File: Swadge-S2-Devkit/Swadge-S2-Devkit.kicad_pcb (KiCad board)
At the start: 2 copper layers, 134 x 100 mm, 102 parts, among them J1 CurrentMonitor, J10 LCD18, J11 LCD28, J2 DEBUG_BANK_C, J3 DEBUG_BANK_B, J4 DEBUG_BANK_A, J5 MICSEL, J6 TRYMIC, J7 LEDK_J, M1 VZ43FC1B5640007L, P1 USB_C_Plug_USB2.0, Q1 Q_N_FET, Q2 AP2003_PN_FET, Q3 AP2003_PN_FET, Q4 AP2003_PN_FET, SW1 4-1437565-2, SW13 touch-ring-6, SW14 SW_SPDT, SW2 4-1437565-2, SW3 4-1437565-2, SW4 4-1437565-2, SW5 4-1437565-2, SW6 4-1437565-2, SW7 4-1437565-2, SW8 4-1437565-2, SW9 4-1437565-2, U1 ESP32-S2-SOLO, U10 GENERIC_LDO_2.8, U11 LCD_240x240_1.3_12, U12 LCD_135x240_1.14_13, U15 LCD_240x240_1.54_12, U2 BUS_PCIexpress, U3 MT3410, U4 GS321-TR, U5 QMA7981, U6 INGHAi_GSPK2308P-8R0.5W, U7 TFT-1.14, U8 TFT_DISPLAY, U9 GENERIC_LDO_1.8

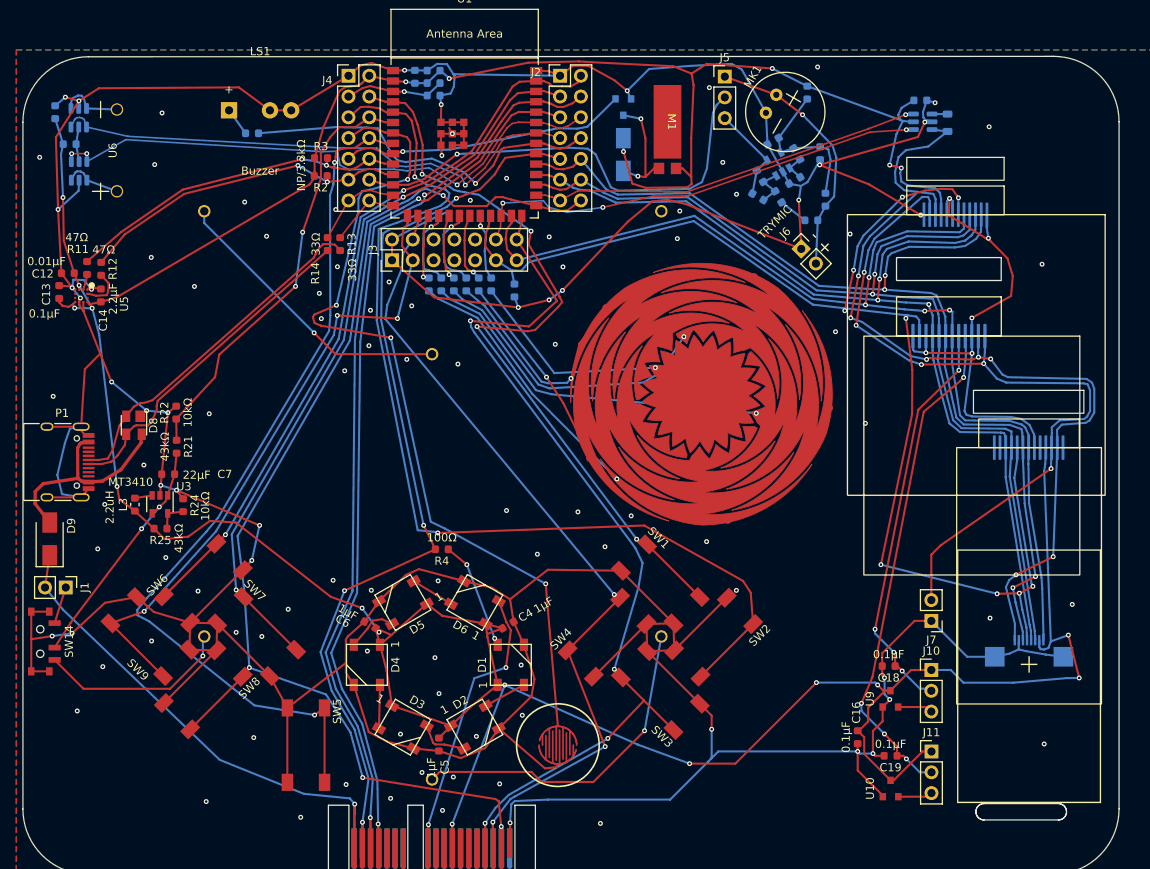
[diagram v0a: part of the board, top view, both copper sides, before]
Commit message: Fixed all import and DRC errors. Cleaned up BOM
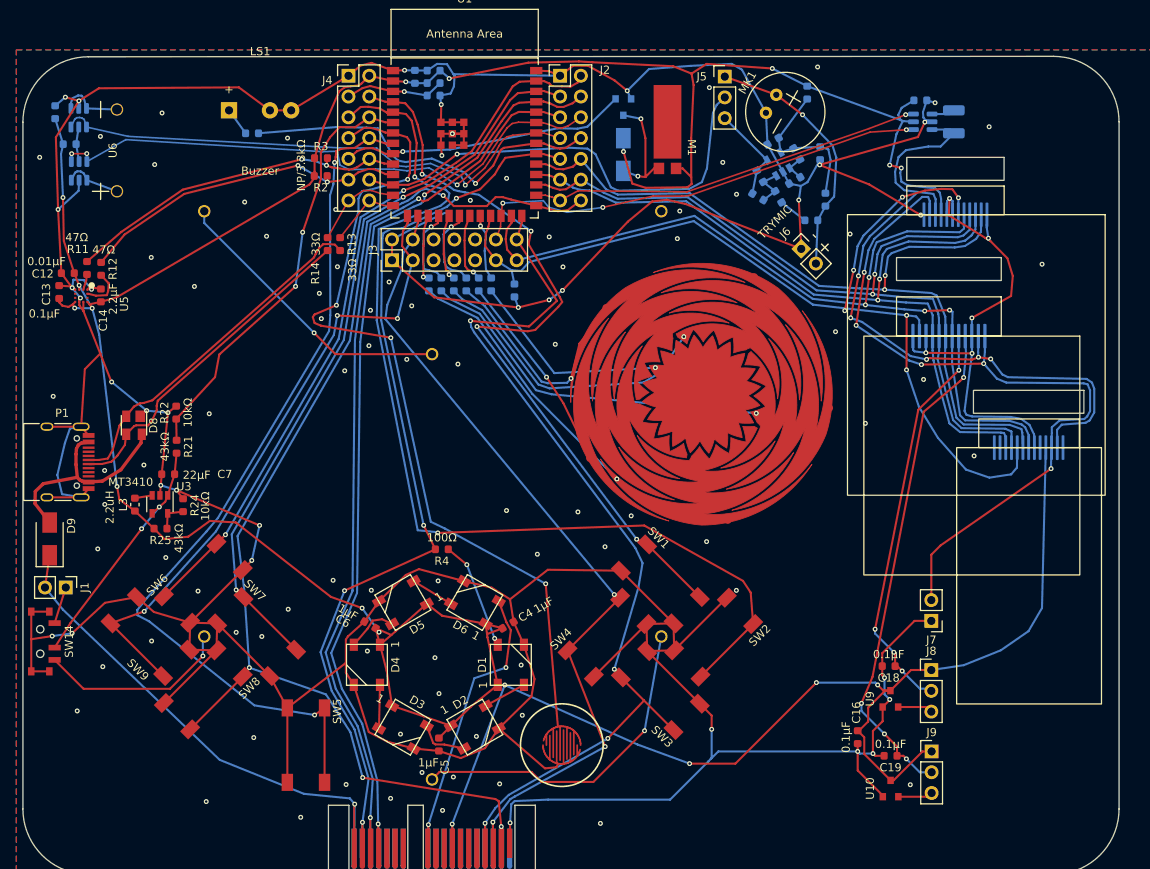
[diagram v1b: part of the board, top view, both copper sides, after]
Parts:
- removed BTN1: BLISTER_SILICONE_BUTTON, Swadge_Parts:BTC007_Button_Silicone
- removed J10: LCD18, Swadge_Parts:PinHeader_1x03_P2.54mm_Vertical
- removed J11: LCD28, Swadge_Parts:PinHeader_1x03_P2.54mm_Vertical
- removed SW13: touch-ring-6, Swadge_Parts:Touch_Teeth_5
- removed U7: TFT-1.14, Swadge_Parts:TFT-1.14
- removed U8: TFT_DISPLAY, Swadge_Parts:NULL
- added J8: LCD18, Swadge_Parts:PinHeader_1x03_P2.54mm_Vertical, F.Cu at (213.4, 126.6)
- added J9: LCD28, Swadge_Parts:PinHeader_1x03_P2.54mm_Vertical, F.Cu at (213.5, 136.6)
- added SW10: BLISTER_SILICONE_BUTTON, Swadge_Parts:BTC007_Button_Silicone, F.Cu at (168.3, 135.8)
- added SW11: touch-ring-6, Swadge_Parts:Touch_Teeth_5, F.Cu at (169.3, 76.9)
- L2: footprint Swadge_Parts:L_0805_2012Metric -> Swadge_Parts:L_1210_3225Metric
- moved L2 0.77 mm to (216.2, 59.6)
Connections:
- P1 pad A8: (no net) -> unconnected-(P1-PadA8)
- P1 pad B6: (no net) -> unconnected-(P1-PadB6)
- P1 pad B7: (no net) -> unconnected-(P1-PadB7)
- P1 pad B8: (no net) -> unconnected-(P1-PadB8)
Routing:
- net TFT_RS: track 165.7 -> 122.8 mm, vias 9 -> 6
- net TFT_RESET: track 125.2 -> 99.7 mm, vias 4 -> 2
- net TFT_LEDA: track 111.4 -> 86.2 mm, vias 7 -> 5
- net TFT_SDA: track 120.2 -> 96.2 mm, vias 3 -> 2
- net TFT_SCL: track 121.0 -> 97.2 mm
- net TFT_CS: track 131.4 -> 107.7 mm
- net GND: track 795.9 -> 775.8 mm, vias 116 -> 119
- net +3V3: track 475.4 -> 458.1 mm, vias 20 -> 18
- net Net-(L2-Pad1): track 1.90 -> 2.85 mm

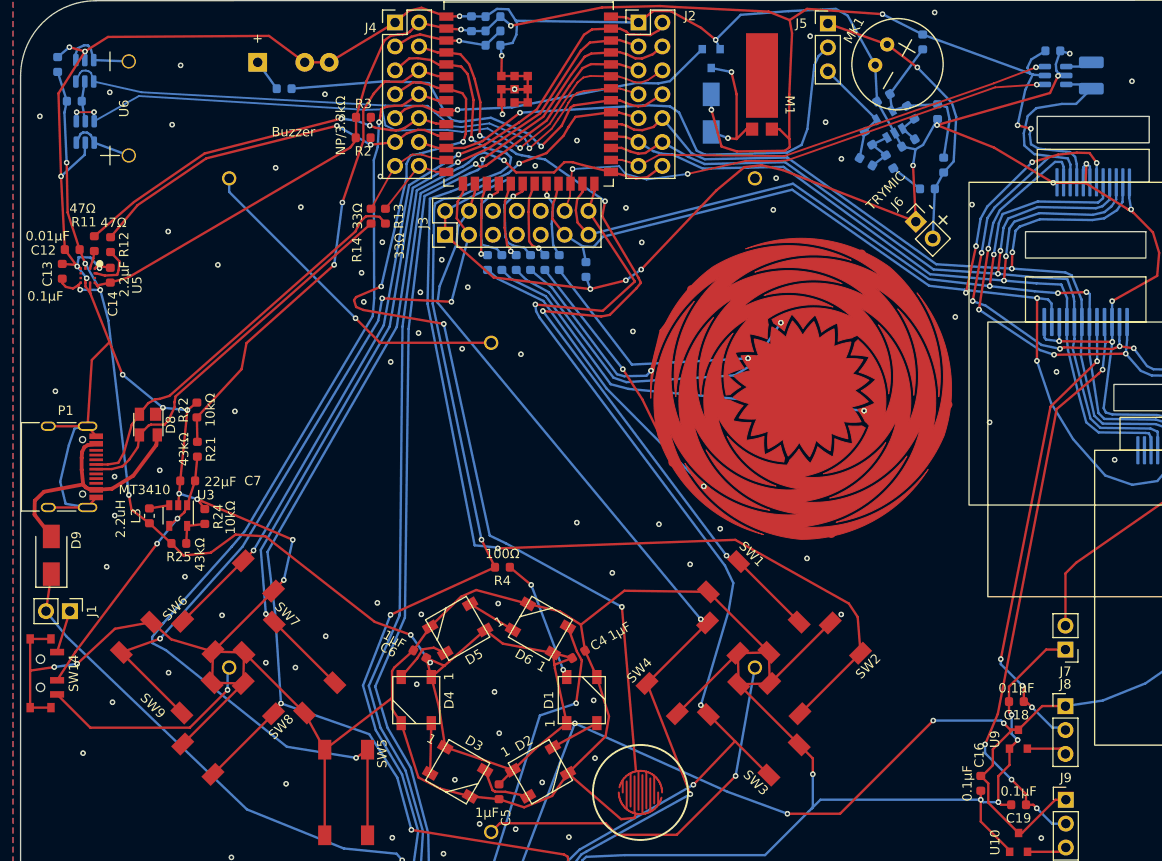
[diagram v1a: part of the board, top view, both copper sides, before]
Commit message: Switch inductors, fix warnings
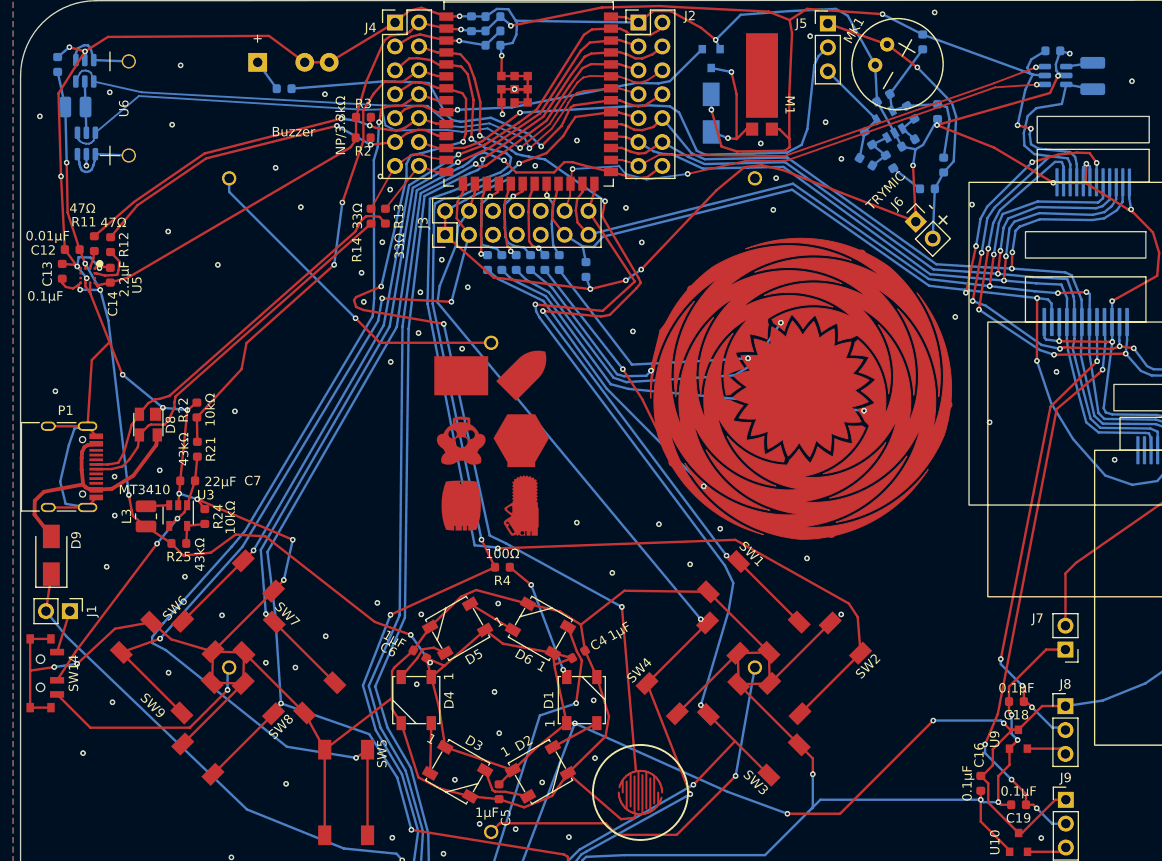
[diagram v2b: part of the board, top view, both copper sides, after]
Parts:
- added Ref**: Val**, Swadge_Parts:swadges-family, F.Cu at (152.5, 98.7)
- L1, L3: footprint Swadge_Parts:L_0603_1608Metric -> Swadge_Parts:L_1008_2520Metric
- moved Q3 1.23 mm to (109.4, 66.8)
- moved L1 0.63 mm to (108.2, 62.9)
- moved L3 0.36 mm to (115.7, 106.5)
- moved L2 0.16 mm to (216.3, 59.7)
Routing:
- net GND: track 775.8 -> 772.3 mm, vias 119 -> 121
- net TFT_LEDA: track 86.2 -> 84.5 mm
- net DIPRAIL: track 4.28 -> 5.45 mm
- net Net-(Q3-Pad4): track 7.05 -> 8.19 mm
- net SP+: track 71.0 -> 71.3 mm, vias 3 -> 1

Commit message: Update note for manufacturing Add silkscreen version Ignore output folder
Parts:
- added svg2mod: G***, Swadge_Parts:MAGFEST_logo_centered_final, F.Cu at (177.1, 146.6)
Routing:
- net GND: vias 121 -> 122
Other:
- board text added: "Swadge S2 Devkit 1.0.0"

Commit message: Reset PCB
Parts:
- removed C12: 0.01μF, Swadge_Parts:C_0603_1608Metric
- removed C13: 0.1μF, Swadge_Parts:C_0603_1608Metric
- removed C14: 2.2μF, Swadge_Parts:C_0603_1608Metric
- removed C15: 10μF, Swadge_Parts:C_0603_1608Metric
- removed D7: D, Swadge_Parts:D_SMA
- removed J1: CurrentMonitor, Swadge_Parts:PinHeader_1x02_P2.54mm_Vertical
- removed J2: DEBUG_BANK_C, Swadge_Parts:PinHeader_2x07_P2.54mm_Vertical
- removed J3: DEBUG_BANK_B, Swadge_Parts:PinHeader_2x07_P2.54mm_Vertical
- removed J4: DEBUG_BANK_A, Swadge_Parts:PinHeader_2x07_P2.54mm_Vertical
- removed L1: 2.2uH, Swadge_Parts:L_1008_2520Metric
- removed M1: VZ43FC1B5640007L, Swadge_Parts:VZ43FC1B5640007L
- removed Q1: Q_N_FET, Swadge_Parts:SOT-23
- removed Q2, Q3: AP2003_PN_FET, Swadge_Parts:SOT-23-6
- removed R11, R12: 47Ω, Swadge_Parts:R_0603_1608Metric
- removed R2, R3: NP/3.3kΩ, Swadge_Parts:R_0603_1608Metric
- removed Ref**: Val**, Swadge_Parts:swadges-family
- removed SW10: BLISTER_SILICONE_BUTTON, Swadge_Parts:BTC007_Button_Silicone
- removed SW14: SW_SPDT, Swadge_Parts:SW_SPDT_PCM12
- removed SW8, SW9: 4-1437565-2, Swadge_Parts:SW_4-1437565-2
- removed U2: BUS_PCIexpress, Swadge_Parts:BUS_PCIexpress
- removed U5: QMA7981, Swadge_Parts:QMA6981
- removed U6: INGHAi_GSPK2308P-8R0.5W, Swadge_Parts:INGHAi GSPK2308P-8R0.5W
- removed svg2mod: G***, Swadge_Parts:MAGFEST_logo_centered_final
- BT1, BT2, BT3, C1, C10, C11, C17, C2, C3, C8, C9, L2, Q4, R1, R10, R15, R16, R17, R18, R19, R20, R23, R26, R5, R6, R7, R8, R9, U11, U12, U15, U4: moved to F.Cu
- SW1, SW2, SW3, SW4, SW5, SW6: value 4-1437565-2 -> EVQ-Q2B03W; footprint Swadge_Parts:SW_4-1437565-2 -> Swadge_Parts:EVQ-Q2B03W
- SW7: value 4-1437565-2 -> SW_SPDT_1825232-1; footprint Swadge_Parts:SW_4-1437565-2 -> Swadge_Parts:1825232-1
- moved L2 158.3 mm to (76.1, 133.1), turned to 0 degrees
- moved Q4 150.2 mm to (81.5, 133.2)
- moved C17 144.1 mm to (90.1, 133.5)
- moved U15 133.5 mm to (84.1, 89.0), turned to 0 degrees
- moved C9 126.9 mm to (94.1, 133.5), turned to 0 degrees
- moved R9 125.9 mm to (86.1, 133.5), turned to 0 degrees
- moved U12 118.5 mm to (107.3, 89.0), turned to 0 degrees
- moved J9 108.3 mm to (119.0, 83.7)
- moved J8 100.1 mm to (119.0, 93.4)
- moved SW1 99.2 mm to (81.7, 127.4), turned to 0 degrees
- moved D5 99.0 mm to (218.9, 48.5), turned to 0 degrees
- moved U4 91.1 mm to (124.8, 123.2), turned to 0 degrees
- moved C11 89.2 mm to (124.4, 126.7), turned to 0 degrees
- moved BT2 83.3 mm to (94.3, 54.3), turned to 0 degrees
- moved C16 82.7 mm to (217.0, 53.0), turned to 0 degrees
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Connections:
- P1 pad B6: unconnected-(P1-PadB6) -> Net-(D8-Pad2)
- P1 pad B7: unconnected-(P1-PadB7) -> Net-(D8-Pad3)
- SW7 pad 1: BTN_7 -> +5V
- SW7 pad 2: BTN_7 -> Net-(C7-Pad1)
- SW7 pad 3: GND -> BATTPLUS
- U1 pad 10: SDA -> unconnected-(U1-Pad10)
- U1 pad 11: SCL -> unconnected-(U1-Pad11)
- U1 pad 15: BTN_9 -> BTN_4
- U1 pad 16: BTN_4 -> unconnected-(U1-Pad16)
- U1 pad 26: BTN_3 -> unconnected-(U1-Pad26)
- U1 pad 27: BTN_8 -> BTN_1
- U1 pad 34: SP- -> unconnected-(U1-Pad34)
- U1 pad 35: SP+ -> unconnected-(U1-Pad35)
- U1 pad 38: BTN_7 -> BTN_3
- U1 pad 39: BTN_6 -> BTN_2
- U1 pad 4: BTN_1 -> BTN_5
- U1 pad 5: BTN_2 -> BTN_6
- U1 pad 7: BLISTER1 -> unconnected-(U1-Pad7)
- U1 pad 8: BTN_5 -> unconnected-(U1-Pad8)
- U1 pad 9: MOTOR -> unconnected-(U1-Pad9)
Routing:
- net GND: track 772.3 -> 0.00 mm, vias 122 -> 0
- net +3V3: track 458.2 -> 0.00 mm, vias 18 -> 0
- net BTN_8: track 144.2 -> 0.00 mm, vias 4 -> 0
- net BTN_2: track 124.1 -> 0.00 mm, vias 2 -> 0
- net TFT_RS: track 122.8 -> 0.00 mm, vias 6 -> 0
- net BTN_3: track 114.9 -> 0.00 mm, vias 4 -> 0
- net TX: track 112.8 -> 0.00 mm, vias 2 -> 0
- net LED: track 112.4 -> 0.00 mm, vias 4 -> 0
- net RX: track 110.6 -> 0.00 mm, vias 2 -> 0
- net BTN_5: track 107.9 -> 0.00 mm, vias 2 -> 0
- net TFT_CS: track 107.7 -> 0.00 mm, vias 4 -> 0
- net BLISTER1: track 103.2 -> 0.00 mm, vias 4 -> 0
- net BTN_4: track 102.7 -> 0.00 mm, vias 3 -> 0
- net TFT_RESET: track 99.7 -> 0.00 mm, vias 2 -> 0
- net TFT_SCL: track 97.2 -> 0.00 mm, vias 2 -> 0
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- removed copper zone on B.Cu, net GND
- removed copper zone on F.Cu, net GND
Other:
- board size 134 x 100 mm -> 13.5 x 2.8 mm
- board text removed: "+ -"
- board text removed: "Swadge S2 Devkit 1.0.0"

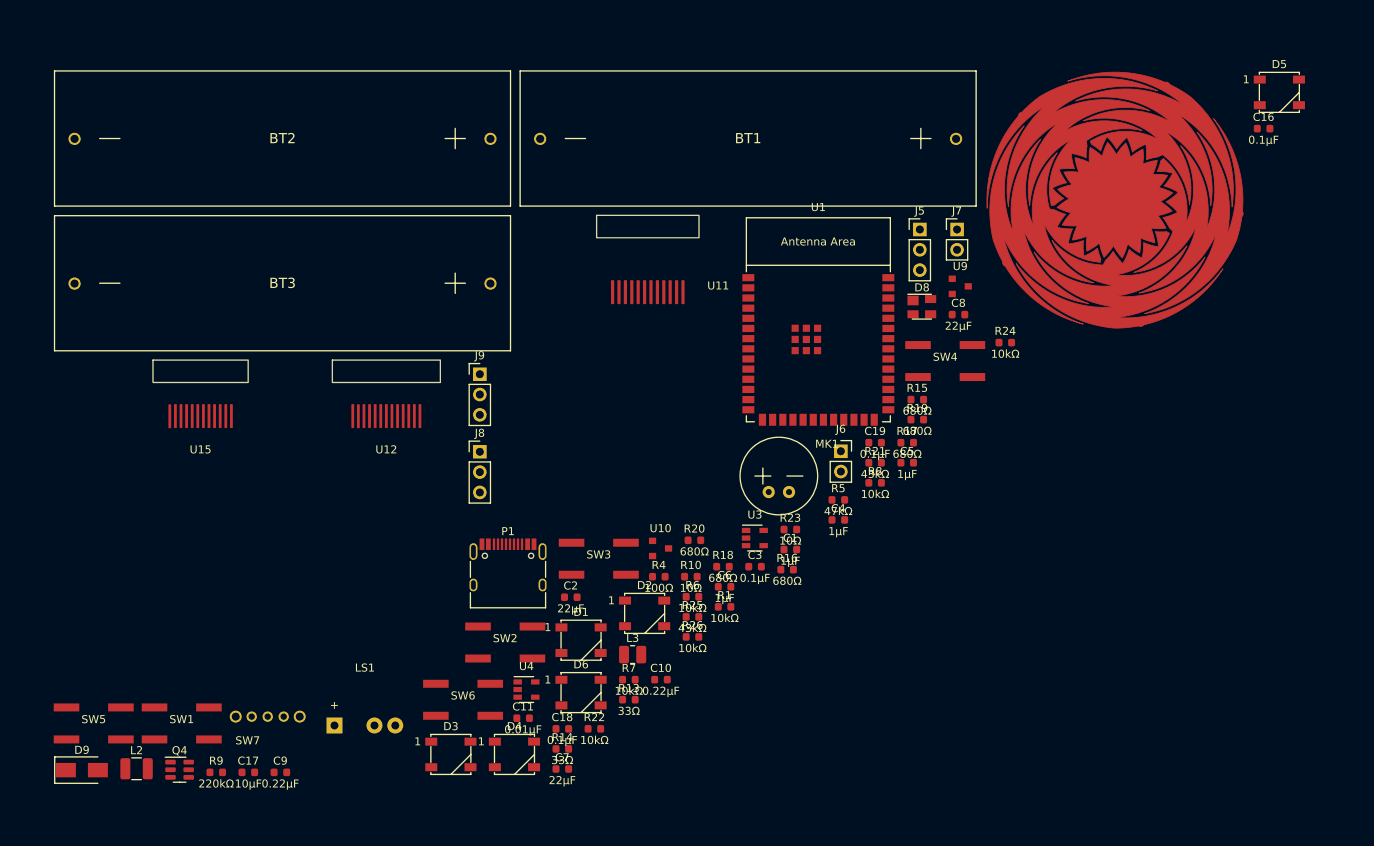
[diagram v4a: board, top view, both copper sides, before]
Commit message: Replaced touch wheel with start/select
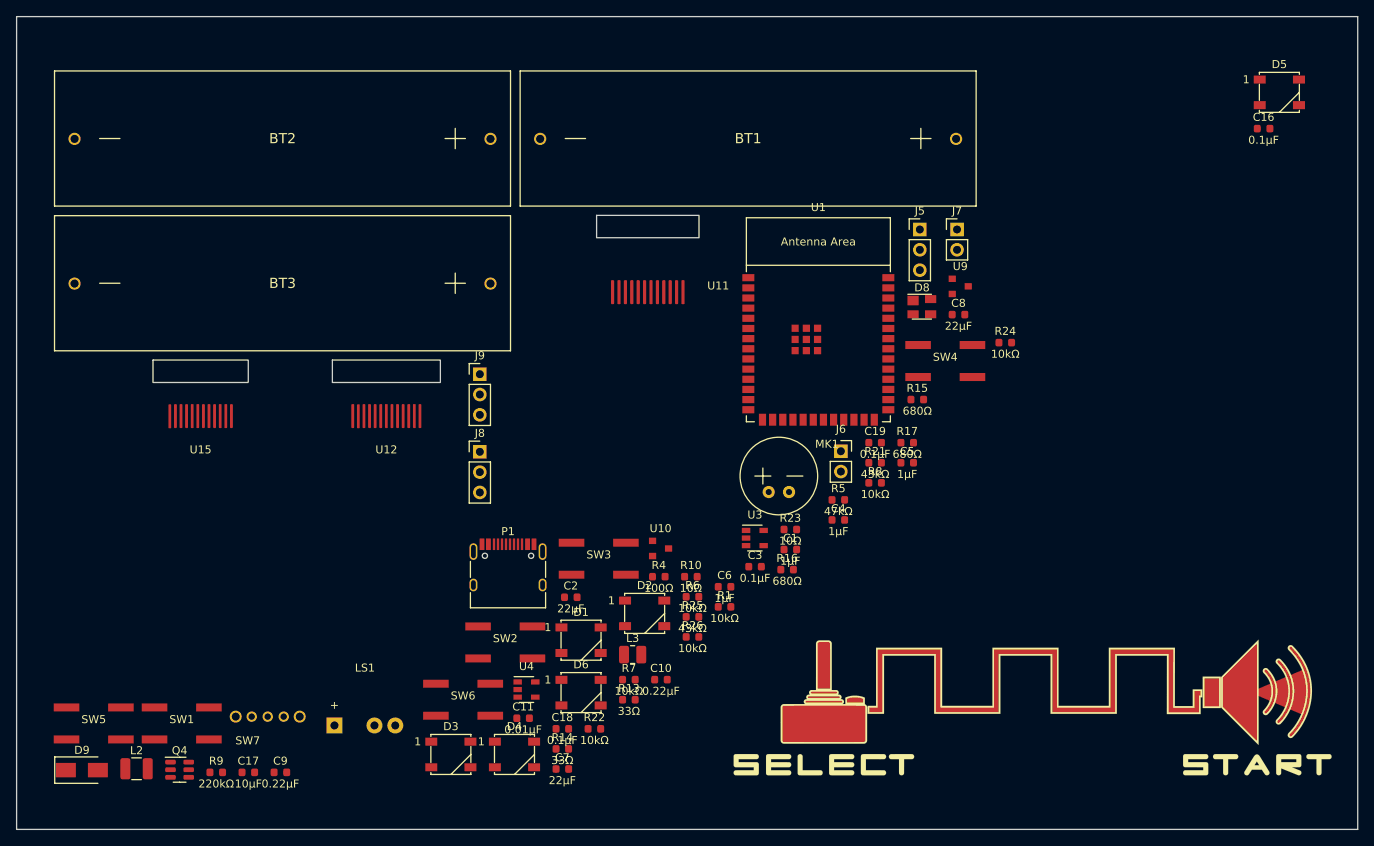
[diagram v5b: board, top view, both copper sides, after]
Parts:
- removed R18, R19, R20: 680Ω, Swadge_Parts:R_0603_1608Metric
- removed SW11: touch-ring-6, Swadge_Parts:Touch_Teeth_5
- added SW8: logo_start_select, Swadge_Parts:start_select, F.Cu at (188.1, 125.4)
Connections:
- U1 pad 20: TOUCH_4 -> unconnected-(U1-Pad20)
- U1 pad 21: TOUCH_5 -> unconnected-(U1-Pad21)
- U1 pad 22: TOUCH_6 -> unconnected-(U1-Pad22)
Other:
- board size 13.5 x 2.8 mm -> 167.6 x 101.6 mm
